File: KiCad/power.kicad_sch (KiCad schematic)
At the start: 33 parts, among them J3 Conn_01x02_Pin, J4 Conn_01x02_Pin, Q1 AO3401A, Q2 AO3401A, Q3 AO3401A, U3 Batter Charger, U4 XC6206PxxxMR, U9 LMV321

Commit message: git Bom power
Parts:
- BT2: cost per unit (none) -> 0
- C1, C2, C3, C4, R2, R3, R4, R5, R7: Extended Part Cost (none) -> 0; cost per unit (none) -> 0,0066
- D1: Extended Part Cost (none) -> 0; cost per unit (none) -> 0,0119
- D2: Extended Part Cost (none) -> 0; cost per unit (none) -> 0,0054
- D4: Extended Part Cost (none) -> 3; cost per unit (none) -> 0,0956
- Q1, Q2, Q3: Extended Part Cost (none) -> 0; cost per unit (none) -> 0,0797
- R14, R18: Extended Part Cost (none) -> 0; cost per unit (none) -> 0,0016
- R15: Extended Part Cost (none) -> 0; cost per unit (none) -> 0,0024
- R16: Extended Part Cost (none) -> 0; cost per unit (none) -> 0,0032
- R17: Extended Part Cost (none) -> 0; cost per unit (none) -> 0,0017
- R19: Extended Part Cost (none) -> 0; cost per unit (none) -> 0,0013
- U3: Extended Part Cost (none) -> 0; cost per unit (none) -> 0,2064
- U4: Extended Part Cost (none) -> 0; cost per unit (none) -> 0,0964
- U9: Extended Part Cost (none) -> 0; cost per unit (none) -> 0,1439

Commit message: bom
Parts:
- D4: value ~ -> zener diode
- J3, J4, JP1: DNF (none) -> X; Extended Part Cost (none) -> 0
- JP2: Extended Part Cost (none) -> 0
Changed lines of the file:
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@@
       (effects (font (size 1.27 1.27)) hide)
     )
-    (property "DNF" "" (at 151.638 24.13 0)
-      (effects (font (size 1.27 1.27)) hide)
-    )
-    (property "Extended Part Cost" "" (at 151.638 24.13 0)
+    (property "DNF" "X" (at 151.638 24.13 0)
+      (effects (font (size 1.27 1.27)) hide)
+    )
+    (property "Extended Part Cost" "0" (at 151.638 24.13 0)
       (effects (font (size 1.27 1.27)) hide)
     )
@@
       (effects (font (size 1.27 1.27)) hide)
     )
-    (property "DNF" "" (at 230.124 143.256 0)
-      (effects (font (size 1.27 1.27)) hide)
-    )
-    (property "Extended Part Cost" "" (at 230.124 143.256 0)
+    (property "DNF" "X" (at 230.124 143.256 0)
+      (effects (font (size 1.27 1.27)) hide)
+    )
+    (property "Extended Part Cost" "0" (at 230.124 143.256 0)
       (effects (font (size 1.27 1.27)) hide)
     )
@@
       (effects (font (size 1.27 1.27)) hide)
     )
-    (property "DNF" "" (at 88.646 93.98 0)
-      (effects (font (size 1.27 1.27)) hide)
-    )
-    (property "Extended Part Cost" "" (at 88.646 93.98 0)
+    (property "DNF" "X" (at 88.646 93.98 0)
+      (effects (font (size 1.27 1.27)) hide)
+    )
+    (property "Extended Part Cost" "0" (at 88.646 93.98 0)
       (effects (font (size 1.27 1.27)) hide)
     )
@@
       (effects (font (size 1.27 1.27)) hide)
     )
-    (property "DNF" "" (at 240.03 91.44 0)
-      (effects (font (size 1.27 1.27)) hide)
-    )
-    (property "Extended Part Cost" "" (at 240.03 91.44 0)
+    (property "DNF" "X" (at 240.03 91.44 0)
+      (effects (font (size 1.27 1.27)) hide)
+    )
+    (property "Extended Part Cost" "0" (at 240.03 91.44 0)
       (effects (font (size 1.27 1.27)) hide)
     )
@@
       (effects (font (size 1.27 1.27)) (justify left))
     )
-    (property "Value" "~" (at 70.358 133.858 0)
+    (property "Value" "zener diode" (at 70.358 133.858 0)
       (effects (font (size 1.27 1.27)))
     )
@@
       (effects (font (size 1.27 1.27)) hide)
     )
-    (property "DNF" "" (at 222.758 24.13 0)
-      (effects (font (size 1.27 1.27)) hide)
-    )
-    (property "Extended Part Cost" "" (at 222.758 24.13 0)
+    (property "DNF" "X" (at 222.758 24.13 0)
+      (effects (font (size 1.27 1.27)) hide)
+    )
+    (property "Extended Part Cost" "0" (at 222.758 24.13 0)
       (effects (font (size 1.27 1.27)) hide)
     )
@@
       (effects (font (size 1.27 1.27)) hide)
     )
-    (property "DNF" "" (at 191.262 37.592 0)
-      (effects (font (size 1.27 1.27)) hide)
-    )
-    (property "Extended Part Cost" "" (at 191.262 37.592 0)
+    (property "DNF" "X" (at 191.262 37.592 0)
+      (effects (font (size 1.27 1.27)) hide)
+    )
+    (property "Extended Part Cost" "0" (at 191.262 37.592 0)
       (effects (font (size 1.27 1.27)) hide)
     )
@@
       (effects (font (size 1.27 1.27)) hide)
     )
-    (property "Extended Part Cost" "" (at 44.45 29.21 0)
-      (effects (font (size 1.27 1.27)) hide)
-    )
+    (property "Extended Part Cost" "0" (at 44.45 29.21 0)
+      (effects (font (size 1.27 1.27)) hide)
+    )

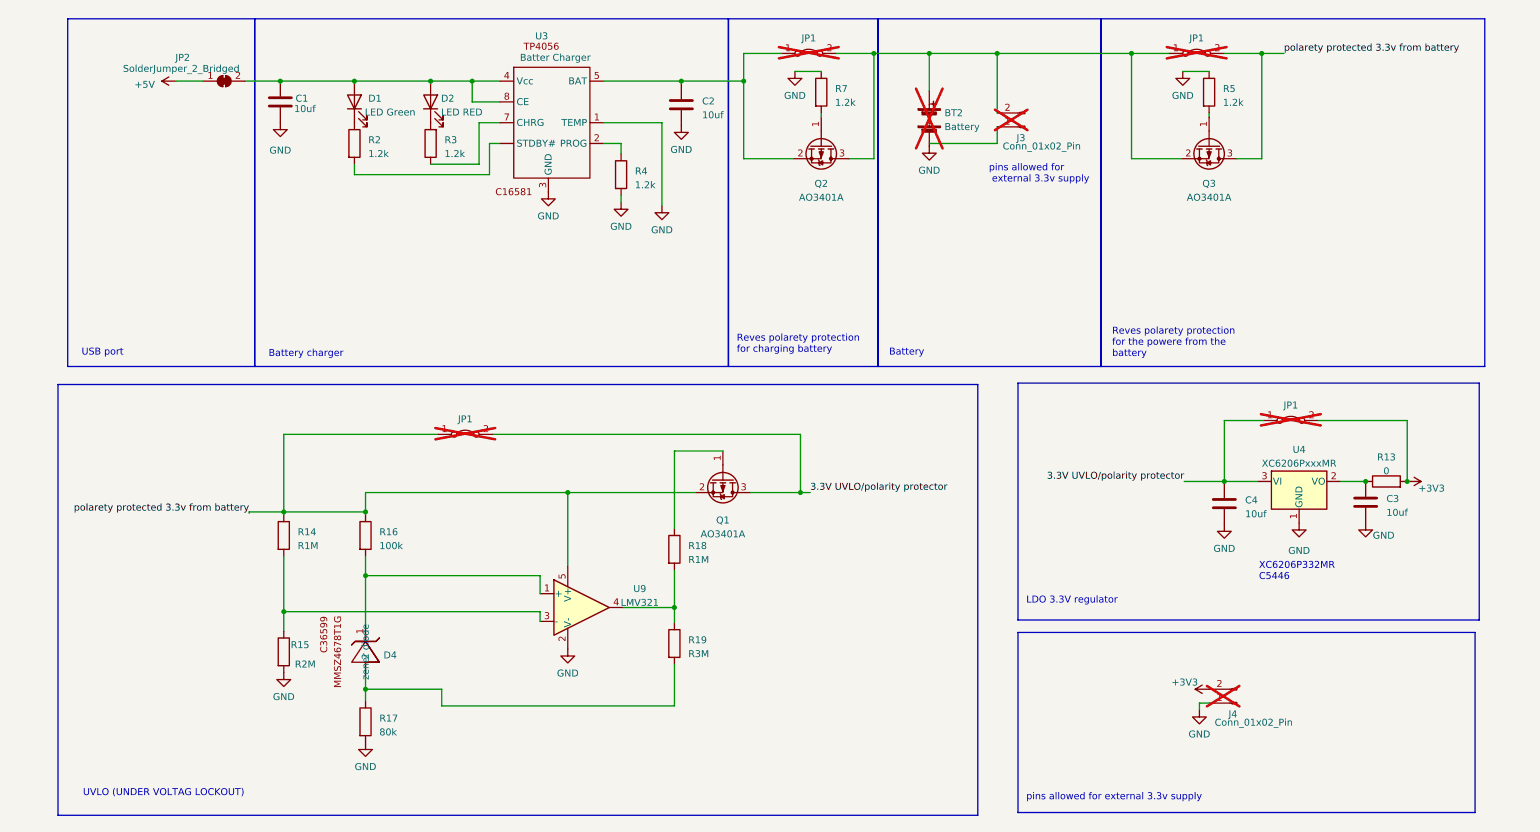
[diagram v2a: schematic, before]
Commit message: power scamatic updated
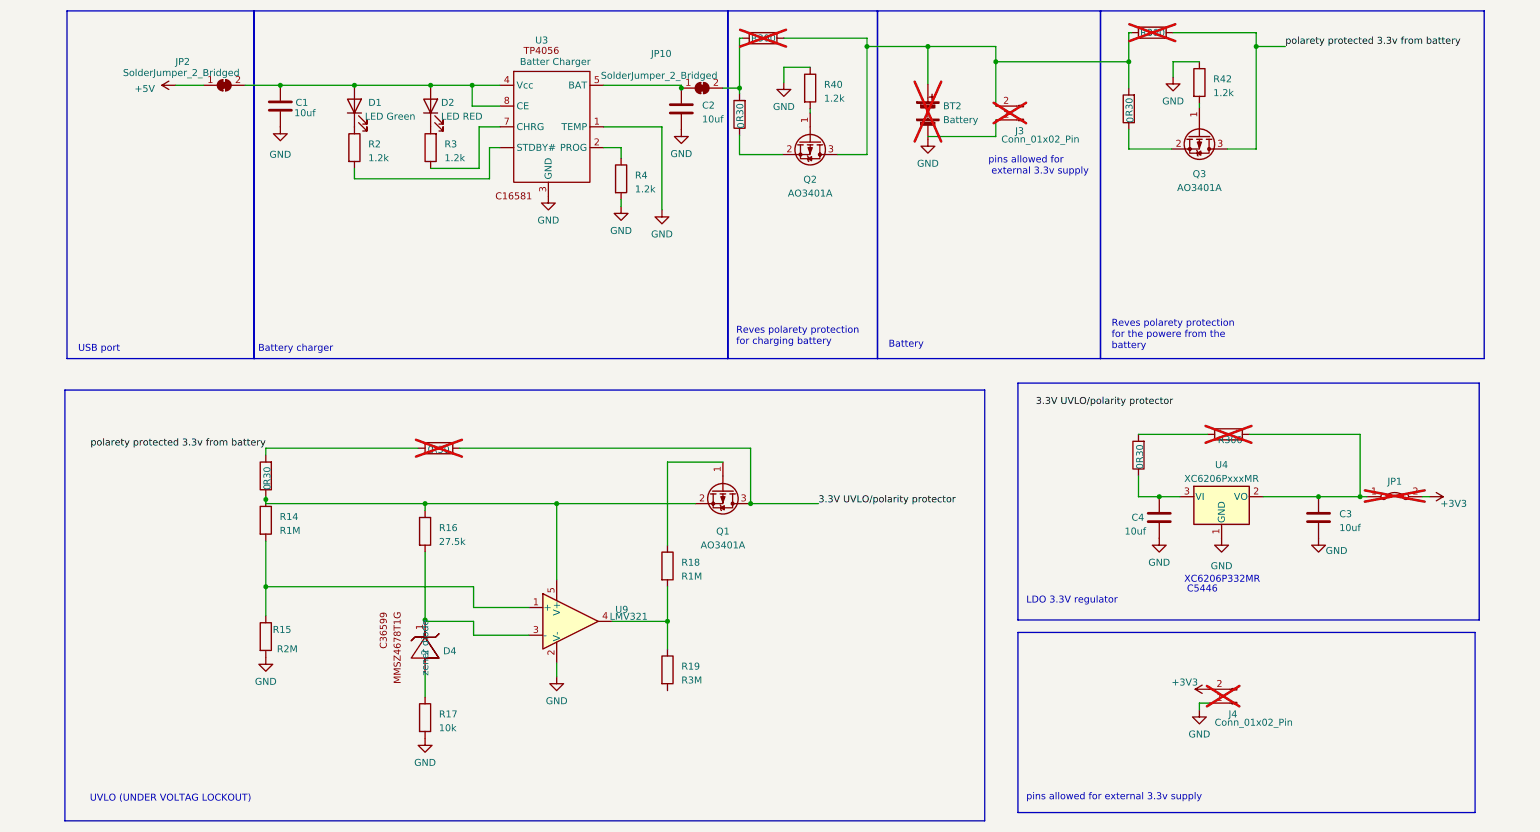
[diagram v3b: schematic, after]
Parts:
- removed JP1 (x4): Jumper_2_Bridged, symbol Jumper:Jumper_2_Bridged
- removed R13: 0, symbol Device:R
- removed R5, R7: 1.2k, symbol Device:R
- added JP1: Jumper_2_Bridged, symbol Jumper:Jumper_2_Bridged
- added JP10: SolderJumper_2_Bridged, symbol Jumper:SolderJumper_2_Bridged
- added R30 (x8): 0, symbol Device:R
- added R40, R42: 1.2k, symbol Device:R
- R16: value 100k -> 27.5k; JLC code C17900 -> C17593; Part name 1206W4F1003T5E -> 0805W8F2702T5E; cost per unit 0,0032 -> 0,0018
- R17: value 80k -> 10k; JLC code C17840 -> C17414; Part name 0805W8F8202T5E -> 0805W8F1002T5E; cost per unit 0,0017 -> 0,0010
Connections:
- net +3V3: now also JP1.2 (B)
- net 3.3V UVLO/polarity protector: no longer C4.1, Q1.3 (D), U4.3 (VI)
- net GND: now also R40.1, R42.1
- net polarety protected 3.3v from battery: now also R30.1, R30.1, R30.2; no longer Q1.2 (S), R14.1, R16.1, U9.5 (V+)
- net at C3.1, U4.2 (VO): now also JP1.1 (A), R30.1
- net at C2.1, U3.5 (BAT): now also JP10.1 (A); no longer Q2.2 (S)
- net at BT2.1 (+), J3.2 (Pin_2), Q2.3 (D): now also R30.1, R30.2, R30.2; no longer Q3.2 (S)
- net at D4. (2), R17.1: no longer R19.2
- net at D4.1, R16.2: now also U9.3 (-); no longer U9.1 (+)
- net at Q3.1 (G): now also R42.2
- net at Q2.1 (G): now also R40.2
- net at R14.2, R15.1: now also U9.1 (+); no longer U9.3 (-)
- new net: JP10.2 (B), R30.2, R30.2
- new net: Q1.2 (S), R14.1, R16.1, R30.1, U9.5 (V+)
- new net: Q1.3 (D), R30.2
- new net: C4.1, R30.1, U4.3 (VI)
- new net: Q3.2 (S), R30.1
- new net: R30.2, R30.2
- new net: Q2.2 (S), R30.1
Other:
- moved on the sheet: BT2, C1, C2, C3, C4, D1, D2, D4, J3, JP2, Q1, R14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

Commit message: power Updated added test points and some 0 ohm resistors as well as trying to fix off-grid problem
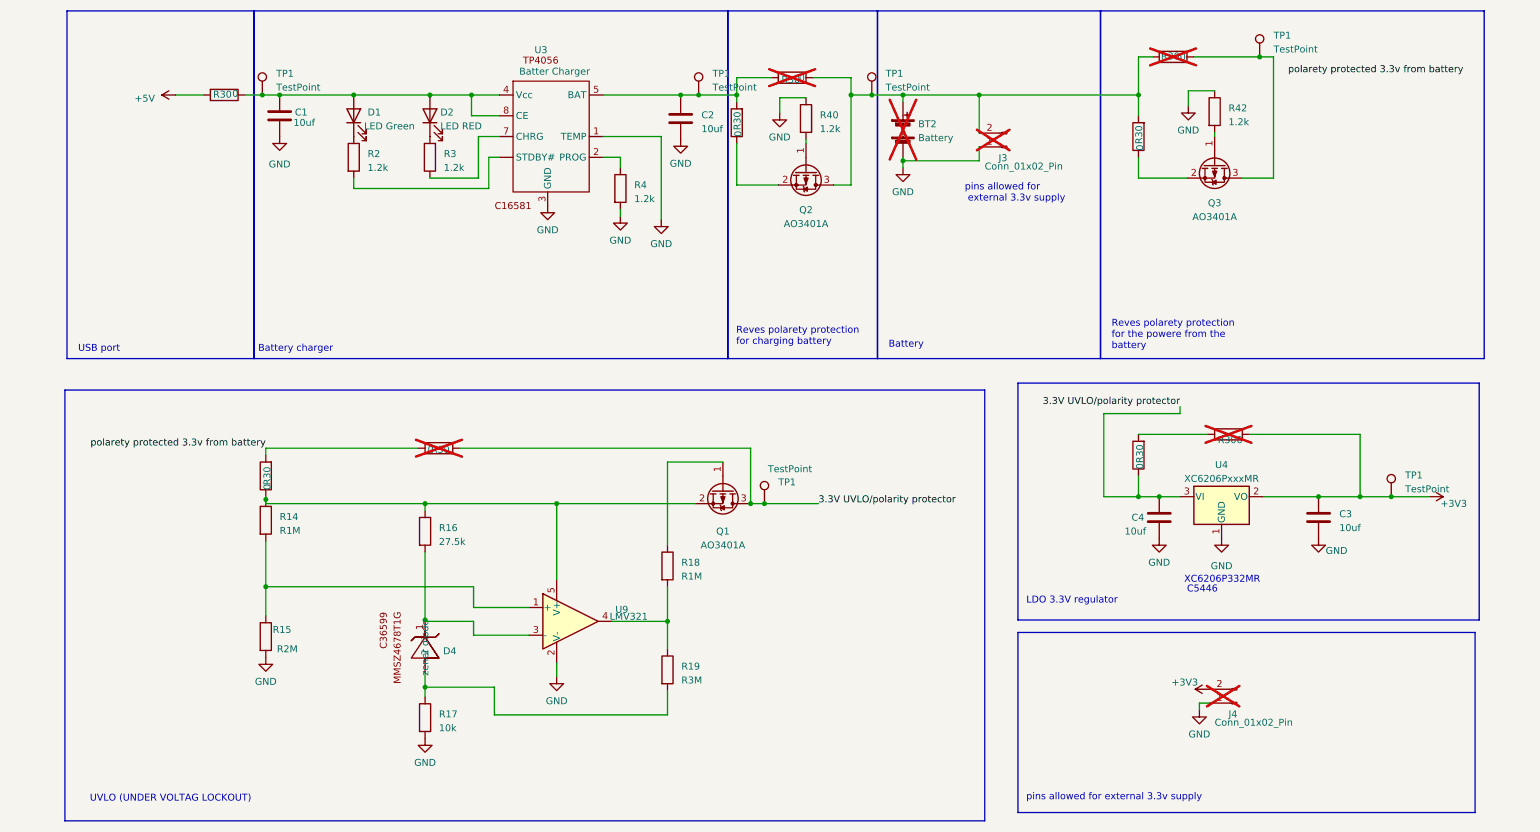
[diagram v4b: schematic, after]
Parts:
- removed JP1: Jumper_2_Bridged, symbol Jumper:Jumper_2_Bridged
- removed JP10, JP2: SolderJumper_2_Bridged, symbol Jumper:SolderJumper_2_Bridged
- removed R30: 0, symbol Device:R
- added R30 (x2): 0, symbol Device:R
- added TP1 (x6): TestPoint, symbol Connector:TestPoint
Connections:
- net +3V3: now also C3.1, R30.1, U4.2 (VO), TP1.1
- net +5V: now also R30.2
- net 3.3V UVLO/polarity protector: now also C4.1, R30.1, U4.3 (VI)
- net GND: now also J3.1 (Pin_1)
- net polarety protected 3.3v from battery: no longer Q3.3 (D), R30.1
- net at C2.1, U3.5 (BAT): now also R30.2, R30.2, TP1.1
- net at C1.1, D1.2 (A), D2.2 (A)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: now also R30.1, TP1.1
- net at Q1.3 (D), R30.2: now also TP1.1
- net at D4. (2), R17.1: now also R19.2
- net at BT2.1 (+), J3.2 (Pin_2), Q2.3 (D)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: now also TP1.1
- net at Q2.2 (S): now also R30.1
- new net: Q3.3 (D), R30.1, TP1.1
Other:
- moved on the sheet: BT2, C1, C2, D1, D2, J3, Q2, Q3, R2, R3, R30, R4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

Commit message: sensors schematic changes, net label name changes
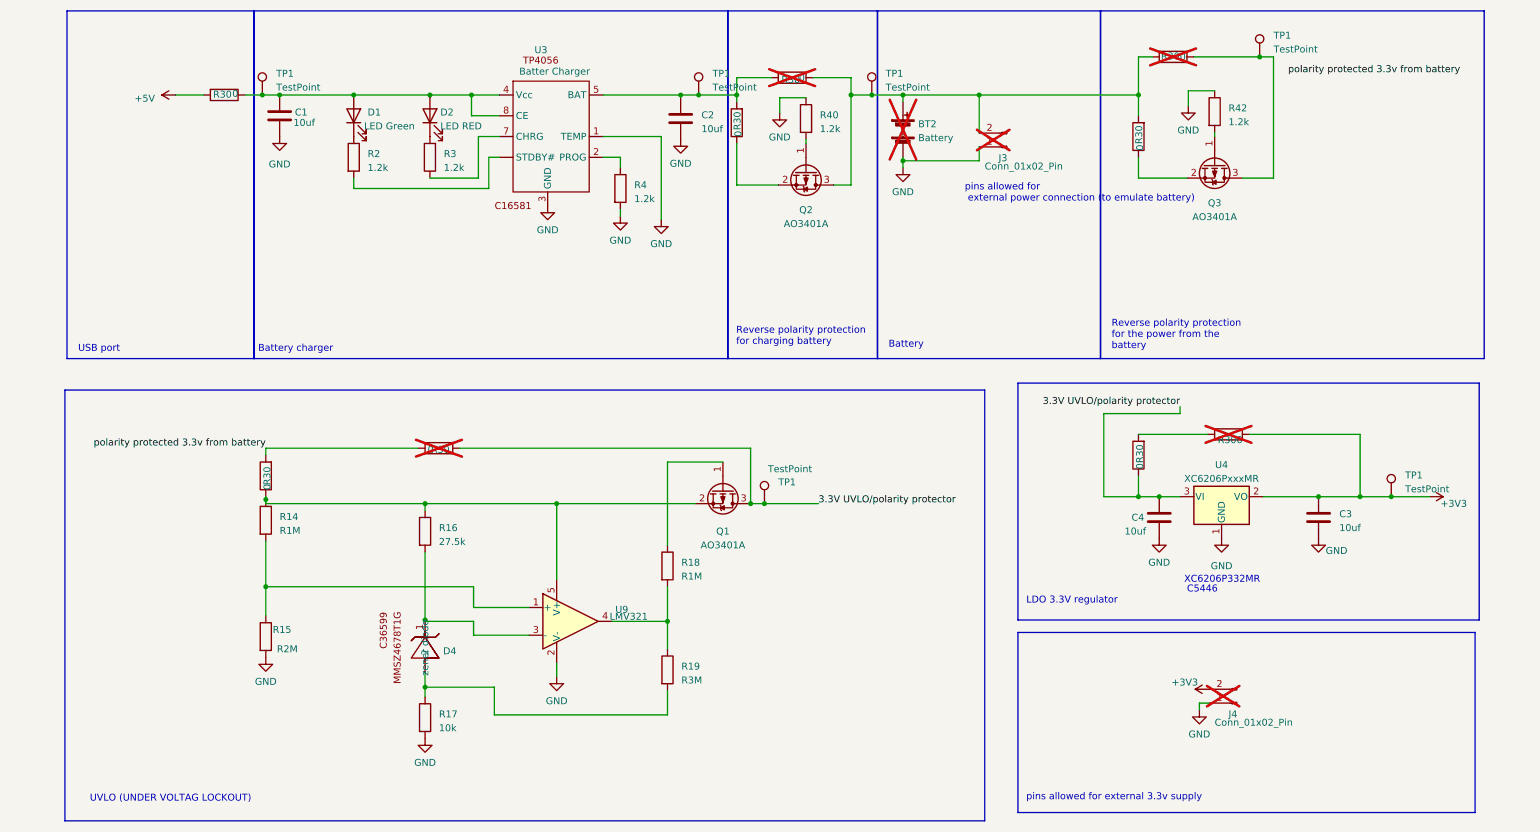
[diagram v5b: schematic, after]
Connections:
- net polarety protected 3.3v from battery renamed polarity protected 3.3v from battery
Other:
- note added: "Reverse polarity protection for charging battery"
- note added: "Reverse polarity protection for the power from the battery"
- note added: "pins allowed for external power connection (to emulate battery)"
- note removed: "Reves polarety protection for charging battery"
- note removed: "Reves polarety protection for the powere from the battery"
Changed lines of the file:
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@@
     (effects (font (size 1.27 1.27)) (justify left bottom))
   )
-  (text "pins allowed for\n external 3.3v supply" (at 180.2384 51.5112 0)
+  (text "pins allowed for\n external power connection (to emulate battery)"
+    (at 180.2384 51.5112 0)
     (effects (font (size 1.27 1.27)) (justify left bottom))
   )
@@
     (effects (font (size 1.27 1.27)) (justify left bottom))
   )
-  (text "Reves polarety protection \nfor the powere from the\nbattery"
+  (text "Reverse polarity protection \nfor the power from the\nbattery"
     (at 207.1624 78.5622 0)
     (effects (font (size 1.27 1.27)) (justify left bottom))
   )
-  (text "Reves polarety protection \nfor charging battery" (at 138.3284 77.8002 0)
+  (text "Reverse polarity protection \nfor charging battery" (at 138.3284 77.8002 0)
     (effects (font (size 1.27 1.27)) (justify left bottom))
   )
@@
     (effects (font (size 1.27 1.27)) (justify left bottom))
   )
-  (label "polarety protected 3.3v from battery" (at 52.07 96.52 180) (fields_autoplaced)
+  (label "polarity protected 3.3v from battery" (at 52.07 96.52 180) (fields_autoplaced)
     (effects (font (size 1.27 1.27)) (justify right bottom))
   )
@@
     (effects (font (size 1.27 1.27)) (justify right bottom))
   )
-  (label "polarety protected 3.3v from battery" (at 239.522 28.067 0) (fields_autoplaced)
+  (label "polarity protected 3.3v from battery" (at 239.522 28.067 0) (fields_autoplaced)
     (effects (font (size 1.27 1.27)) (justify left bottom))
   )

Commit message: changed a bunch of net labels, changed some uc schem stuff
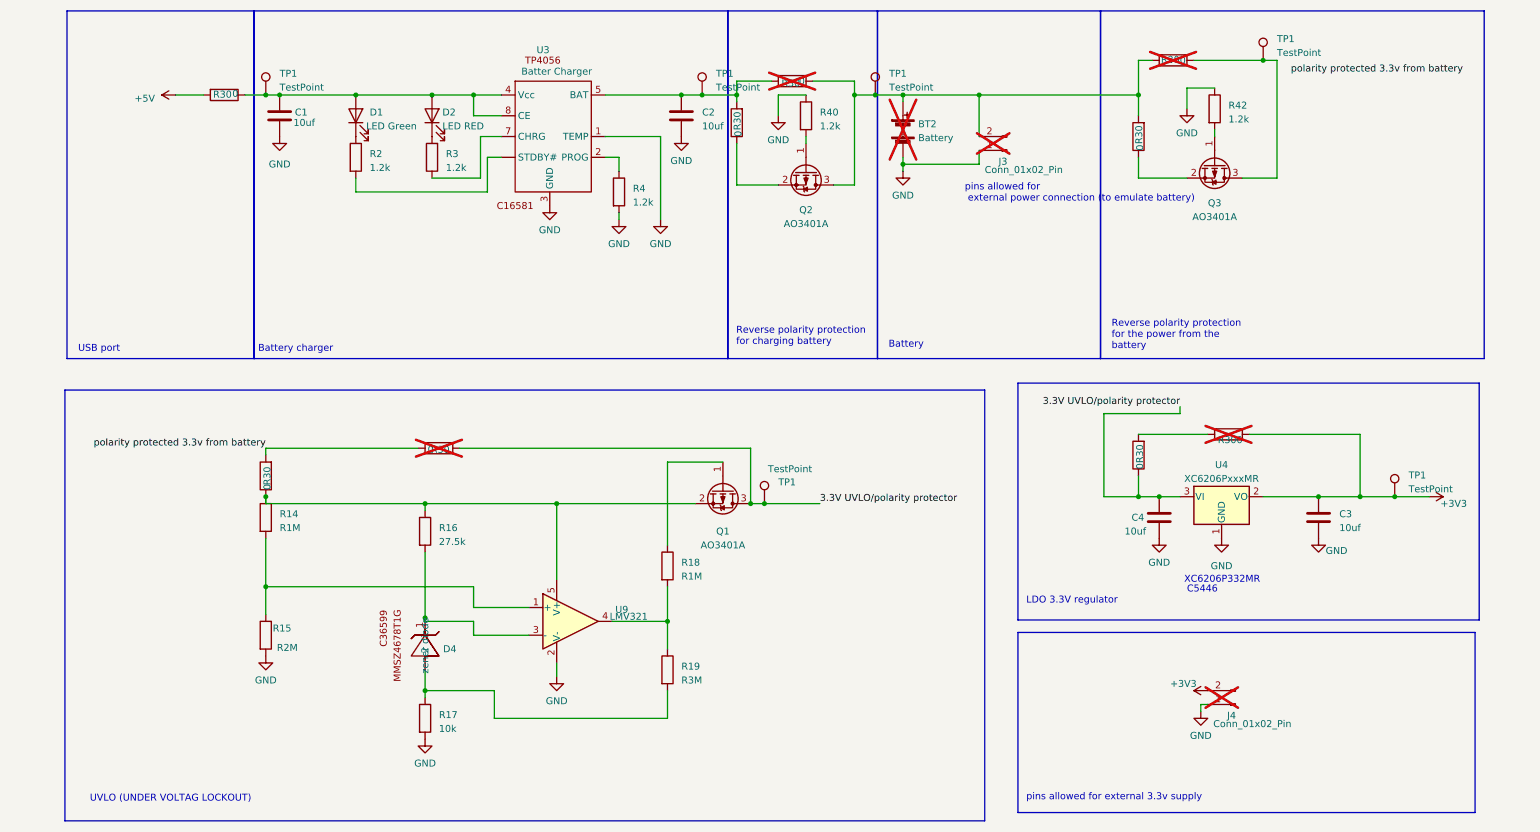
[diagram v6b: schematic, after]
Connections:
- net 3.3V UVLO/polarity protector: now also Q1.3 (D), R30.2, TP1.1
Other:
- moved on the sheet: C2, J3, R14, R30, R4, R40, R42, TP1

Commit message: power final chang
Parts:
- renumbered BT2 to BT?, C4 to C?, C2 to C?, C3 to C?, C1 to C?, D2 to D?, D1 to D?, D4 to D?, J4 to J?, J3 to J?, Q1 to Q?, Q3 to Q?, Q2 to Q?, R40 to R?, R17 to R?, R16 to R?, R18 to R?, R2 to R?, R30 to R?, R15 to R?, R19 to R?, R14 to R?, R42 to R?, R4 to R?, R3 to R?, TP1 to TP?, U4 to U?, U9 to U?, U3 to U?
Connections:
- net polarity protected 3.3v from battery: now also Q?.3 (D), R?.1, TP?.1
